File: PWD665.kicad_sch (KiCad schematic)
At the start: 0 parts

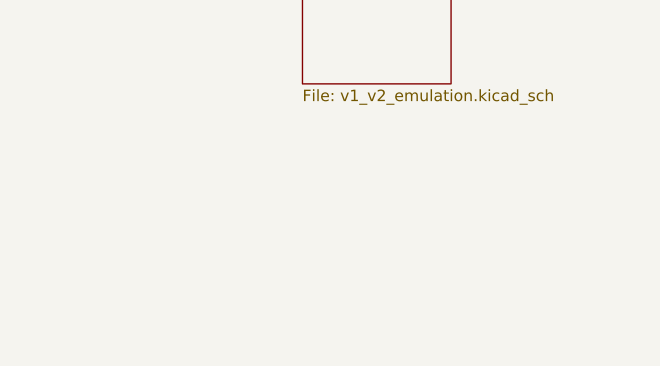
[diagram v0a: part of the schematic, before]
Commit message: add CN2 FDD connector
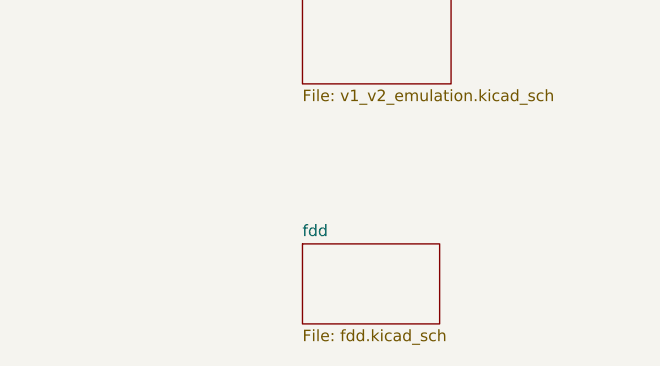
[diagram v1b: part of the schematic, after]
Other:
- added sheet fdd (fdd.kicad_sch)
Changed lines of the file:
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@@
+    )
+  )
+  (sheet (at 125.73 87.63) (size 15.24 8.89) (fields_autoplaced)
+    (stroke (width 0.1524) (type solid))
+    (fill (color 0 0 0 0.0000))
+    (property "Sheetname" "fdd" (at 125.73 86.9184 0)
+      (effects (font (size 1.27 1.27)) (justify left bottom))
+    )
+    (property "Sheetfile" "fdd.kicad_sch" (at 125.73 97.1046 0)
+      (effects (font (size 1.27 1.27)) (justify left top))
+    )
+    (instances
+      (project "PWD665"
+        (path "/8cd193ae-a369-4130-9ba4-f2075fa60e2b" (page "4"))
+      )
     )
   )

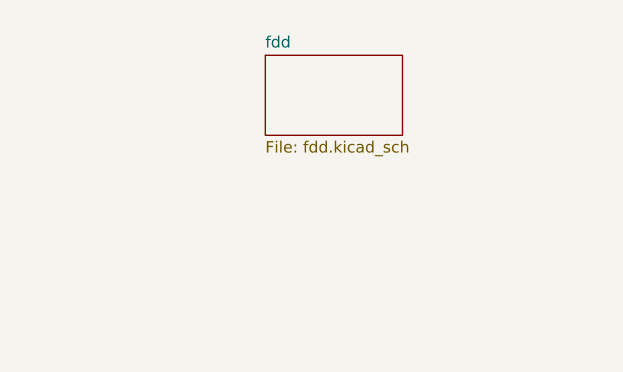
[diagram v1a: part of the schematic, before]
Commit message: add CN4 TEXT BUS
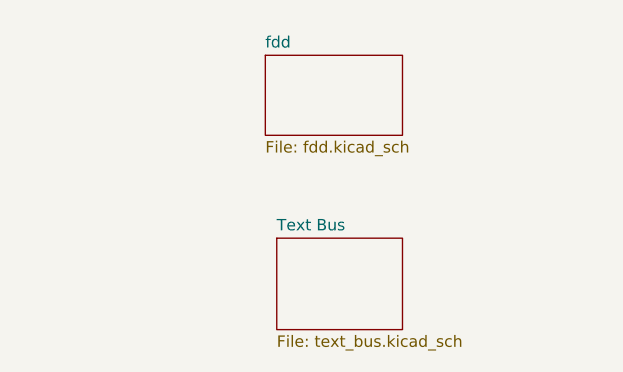
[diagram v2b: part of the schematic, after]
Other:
- added sheet Text Bus (text_bus.kicad_sch)
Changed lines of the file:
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@@
+    )
+  )
+  (sheet (at 127 107.95) (size 13.97 10.16) (fields_autoplaced)
+    (stroke (width 0.1524) (type solid))
+    (fill (color 0 0 0 0.0000))
+    (property "Sheetname" "Text Bus" (at 127 107.2384 0)
+      (effects (font (size 1.27 1.27)) (justify left bottom))
+    )
+    (property "Sheetfile" "text_bus.kicad_sch" (at 127 118.6946 0)
+      (effects (font (size 1.27 1.27)) (justify left top))
+    )
+    (instances
+      (project "PWD665"
+        (path "/8cd193ae-a369-4130-9ba4-f2075fa60e2b" (page "5"))
+      )
     )
   )
